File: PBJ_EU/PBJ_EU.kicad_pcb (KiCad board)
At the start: 2 copper layers, 111.4 x 128.5 mm, 75 parts, among them J1 Molex_47257, J10 Conn_02x05_Odd_Even, J2 Molex_47257, J3 Molex_47257, J4 Molex_47257, J7 Conn_02x05_Odd_Even, J9 Conn_02x08_Odd_Even_Female, SW1 SW_SPDT, SW2 SW_SPDT, SW5 SW_DPST, U1 TL072, U2 TL072, U7 MC7805CTG

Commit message: Version 4.10
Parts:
- U7: footprint Package_TO_SOT_THT:TO-220-3_Vertical -> Package_TO_SOT_THT:TO-220-3_Horizontal_TabDown
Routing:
- net +12V: track 0.00 -> 182.8 mm, vias 0 -> 5
- added copper zone on B.Cu, net GND
- removed copper zone on B.Cu, net +12V

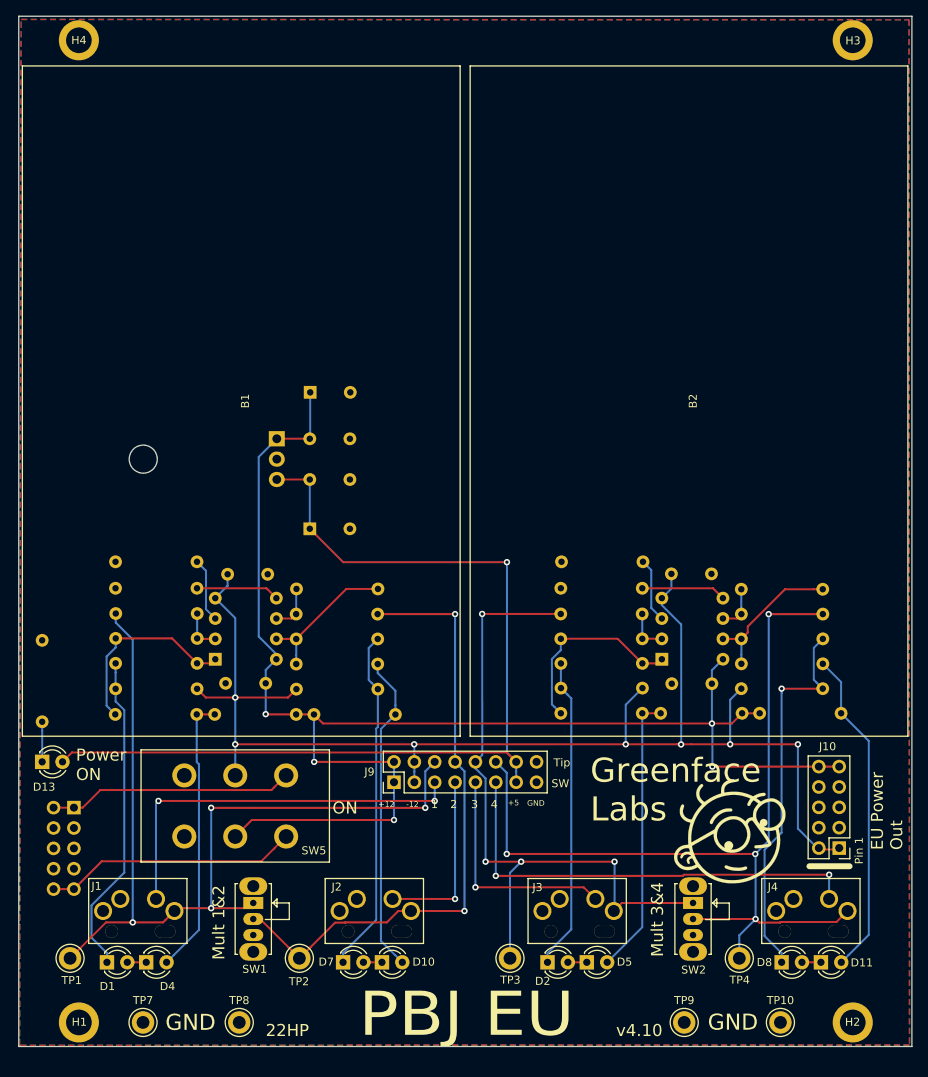
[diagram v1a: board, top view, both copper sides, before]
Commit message: v5.2
Adds LCSC build support. Fixes to monitor circuitry.
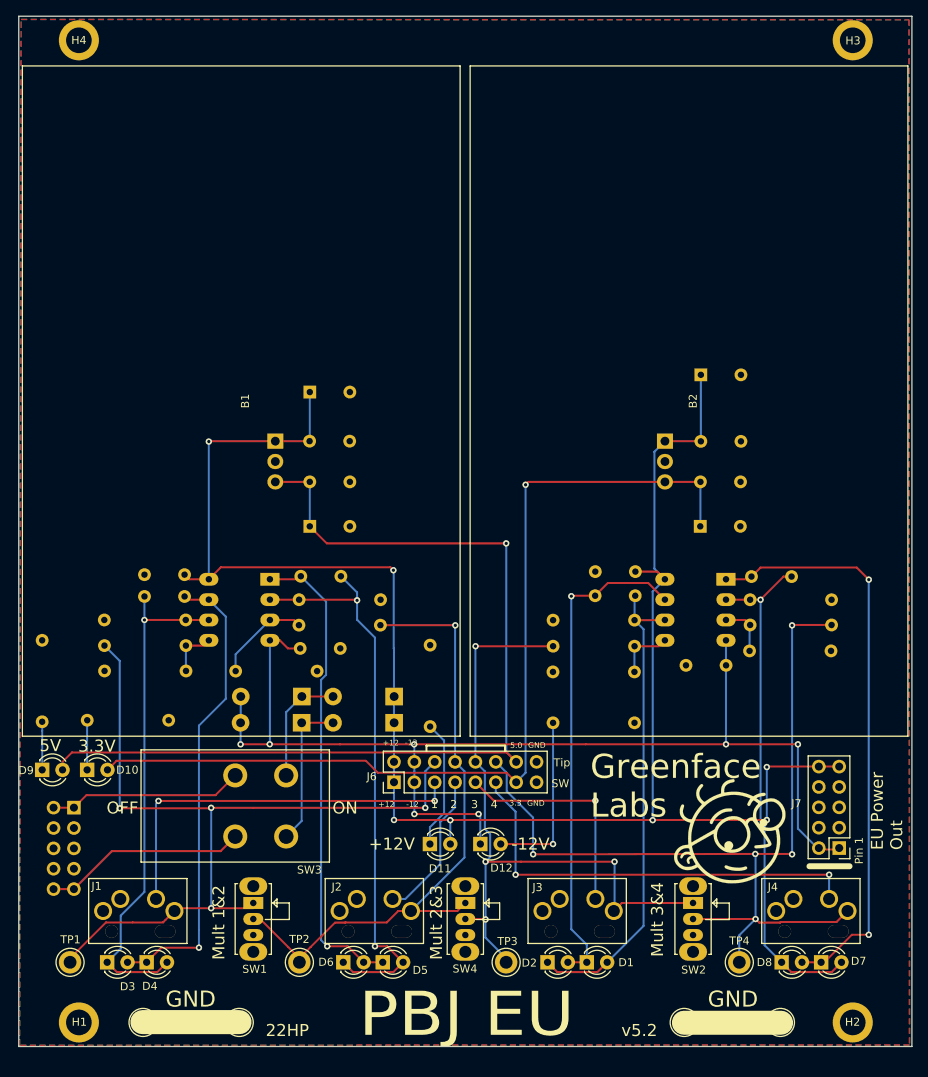
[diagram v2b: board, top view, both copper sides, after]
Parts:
- removed D13: GREEN LED, LED_THT:LED_D3.0mm
- removed J10: Conn_02x05_Odd_Even, Connector_PinHeader_2.54mm:PinHeader_2x05_P2.54mm_Vertical
- removed J9: Conn_02x08_Odd_Even_Female, Connector_PinHeader_2.54mm:PinHeader_2x08_P2.54mm_Vertical
- removed R17, R40, R41: 3.32M, Resistor_THT:R_Axial_DIN0207_L6.3mm_D2.5mm_P10.16mm_Horizontal
- removed R19, R20, R31, R32, R44, R45: 10K, Resistor_THT:R_Axial_DIN0207_L6.3mm_D2.5mm_P10.16mm_Horizontal
- removed R22, R23, R43, R47, R48: 2.2K, Resistor_THT:R_Axial_DIN0207_L6.3mm_D2.5mm_P10.16mm_Horizontal
- removed R34, R35: 1.00M, Resistor_THT:R_Axial_DIN0207_L6.3mm_D2.5mm_P10.16mm_Horizontal
- removed R37, R38: 1K, Resistor_THT:R_Axial_DIN0207_L6.3mm_D2.5mm_P10.16mm_Horizontal
- removed SW5: SW_DPST, sputterizer:S202031MS02Q
- removed TP10, TP9: TestPoint, TestPoint:TestPoint_Keystone_5005-5009_Compact
- removed U7: MC7805CTG, Package_TO_SOT_THT:TO-220-3_Horizontal_TabDown
- added C10: .1uF, Capacitor_THT:C_Rect_L7.0mm_W2.0mm_P5.00mm, B.Cu at (116.9, 99.3)
- added C11: .1uF, Capacitor_THT:C_Rect_L7.0mm_W2.0mm_P5.00mm, B.Cu at (123.2, 111.0)
- added C12: 10uF, Capacitor_THT:CP_Radial_Tantal_D5.0mm_P5.00mm, B.Cu at (125.0, 93.6)
- added C13: 10nF, Capacitor_THT:C_Rect_L7.0mm_W2.0mm_P5.00mm, B.Cu at (116.9, 102.3)
- added C14: 10nF, Capacitor_THT:C_Rect_L7.0mm_W2.0mm_P5.00mm, B.Cu at (55.7, 102.4)
- added C15: 10nF, Capacitor_THT:C_Rect_L7.0mm_W2.0mm_P5.00mm, B.Cu at (80.2, 99.8)
- added C16: 10nF, Capacitor_THT:C_Rect_L7.0mm_W2.0mm_P5.00mm, B.Cu at (136.4, 99.9)
- added C9: .1uF, Capacitor_THT:C_Rect_L7.0mm_W2.0mm_P5.00mm, B.Cu at (125.0, 88.1)
- added D12: GREEN LED, LED_THT:LED_D3.0mm, F.Cu at (97.6, 133.2)
- added D18: SB120, Diode_THT:D_DO-41_SOD81_P7.62mm_Horizontal, B.Cu at (86.8, 118.1)
- added D19: SB120, Diode_THT:D_DO-41_SOD81_P7.62mm_Horizontal, B.Cu at (86.8, 114.8)
- added D20: SB120, Diode_THT:D_DO-41_SOD81_P7.62mm_Horizontal, B.Cu at (75.3, 118.1)
- added D21: SB120, Diode_THT:D_DO-41_SOD81_P7.62mm_Horizontal, B.Cu at (75.3, 114.8)
- added D3: RED LED, LED_THT:LED_D3.0mm, F.Cu at (51.0, 148.0)
- added D6: RED LED, LED_THT:LED_D3.0mm, F.Cu at (80.5, 148.0)
- added D9: GREEN LED, LED_THT:LED_D3.0mm, F.Cu at (42.9, 124.0)
- added J5: Conn_02x05_Odd_Even, Connector_PinHeader_2.54mm:PinHeader_2x05_P2.54mm_Vertical, B.Cu at (46.9, 128.7)
- added J6: Conn_02x08_Odd_Even_Female, Connector_PinHeader_2.54mm:PinHeader_2x08_P2.54mm_Vertical, F.Cu at (86.8, 125.5)
- added R12: 1M, Resistor_THT:R_Axial_DIN0207_L6.3mm_D2.5mm_P10.16mm_Horizontal, B.Cu at (67.0, 111.7)
- added R15: 2.2K, Resistor_THT:R_Axial_DIN0207_L6.3mm_D2.5mm_P10.16mm_Horizontal, B.Cu at (91.3, 118.6)
- added R5: 2.2K, Resistor_THT:R_Axial_DIN0207_L6.3mm_D2.5mm_P10.16mm_Horizontal, B.Cu at (42.9, 118.0)
- added R6: 2.2K, Resistor_THT:R_Axial_DIN0207_L6.3mm_D2.5mm_P10.16mm_Horizontal, B.Cu at (60.9, 108.5)
- added R9: 2.2K, Resistor_THT:R_Axial_DIN0207_L6.3mm_D2.5mm_P10.16mm_Horizontal, B.Cu at (131.2, 105.9)
- added SW3: SW_DPST, sputterizer:S202031MS02Q, F.Cu at (67.0, 128.5)
- added SW4: SW_SPDT, Button_Switch_THT:SW_Slide_1P2T_CK_OS102011MS2Q, F.Cu at (95.7, 140.6)
- added TP5: TestPoint, TestPoint:TestPoint_Keystone_5005-5009_Compact, F.Cu at (123.0, 155.5)
- added TP6: TestPoint, TestPoint:TestPoint_Keystone_5005-5009_Compact, F.Cu at (135.0, 155.5)
- added U3: MC7805CTG, Package_TO_SOT_THT:TO-220-3_Vertical, B.Cu at (72.0, 83.0)
- added U4: MIC29150-3.3WT, Package_TO_SOT_THT:TO-220-3_Vertical, B.Cu at (120.6, 83.0)
- C2: value 10uF -> .33uF; footprint Capacitor_THT:CP_Radial_Tantal_D5.0mm_P5.00mm -> Capacitor_THT:C_Rect_L7.0mm_W2.0mm_P5.00mm
- C3: value .33uF -> .1uF
- C4, C5: value .1uF -> 10uF; footprint Capacitor_THT:C_Rect_L7.0mm_W2.0mm_P5.00mm -> Capacitor_THT:CP_Radial_Tantal_D5.0mm_P5.00mm
- C8: value .1uF -> .33uF
- D1, D7: value RED LED -> BLUE LED
- D10, D11: value BLUE LED -> GREEN LED
- J7: moved to F.Cu
- R1, R2, R3, R4: value 750K -> 2.2K
- R10, R11: value 1.00M -> 1M
- R13: value 1K -> 1M
- R14: value 1K -> 2.2K
- R16: value 3.32M -> 2.2K
- R7, R8: value 10K -> 2.2K
- U1, U2: value TL072 -> TL032IP; footprint Package_DIP:DIP-8_W7.62mm -> Package_DIP:DIP-8_W7.62mm_Socket_LongPads
- moved J7 95.6 mm to (142.3, 133.8)
- moved R14 69.6 mm to (48.5, 117.8), turned to 0 degrees
- moved R13 68.9 mm to (131.2, 109.2), turned to 0 degrees
- moved R2 67.6 mm to (50.7, 105.3), turned to 0 degrees
- moved C6 67.2 mm to (60.7, 99.7)
- moved R10 65.1 mm to (116.8, 111.8), turned to 180 degrees
- moved R7 64.9 mm to (116.8, 108.6), turned to 180 degrees
- moved D1 59.8 mm to (110.8, 148.0)
- moved D7 59.6 mm to (140.1, 148.0)
- moved C5 59.5 mm to (125.1, 74.7), turned to 0 degrees
- moved D11 50.9 mm to (91.3, 133.2)
- moved C8 49.0 mm to (125.1, 83.0)
- moved R11 47.3 mm to (60.9, 111.7), turned to 180 degrees
- moved C7 47.2 mm to (80.1, 108.8)
- moved R16 45.6 mm to (106.6, 118.1), turned to 0 degrees
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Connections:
- C2 pad 1: +5V -> +12V
- C3 pad 1: +12V -> +5V
- C4 pad 1: +12V -> +5V
- C5 pad 1: GND -> +12V
- C5 pad 2: -12V -> GND
- C8 pad 1: +5V -> +12V
- D1 pad 2: GND -> Net-(D1-Pad2)
- D10 pad 1: GND -> Net-(D10-Pad1)
- D10 pad 2: Net-(D10-Pad2) -> +3V3
- D11 pad 1: GND -> Net-(D11-Pad1)
- D11 pad 2: Net-(D11-Pad2) -> +12V
- D2 pad 1: Net-(D2-Pad1) -> Net-(D1-Pad2)
- D2 pad 2: GND -> Net-(D1-Pad1)
- D4 pad 1: GND -> Net-(D3-Pad2)
- D4 pad 2: Net-(D4-Pad2) -> Net-(D3-Pad1)
- D5 pad 1: GND -> Net-(D5-Pad1)
- D7 pad 2: GND -> Net-(D7-Pad2)
- D8 pad 1: Net-(D8-Pad1) -> Net-(D7-Pad2)
- D8 pad 2: GND -> Net-(D7-Pad1)
- J7 pad 1: Net-(J7-Pad1) -> -12V
- J7 pad 10: Net-(J7-Pad10) -> +12V
- J7 pad 2: Net-(J7-Pad1) -> -12V
- J7 pad 9: Net-(J7-Pad10) -> +12V
- R1 pad 1: Net-(R1-Pad1) -> GND
- R1 pad 2: GND -> Net-(D1-Pad2)
- R10 pad 1: Tip1 -> Net-(R10-Pad1)
- R10 pad 2: Net-(R10-Pad2) -> GND
- R11 pad 1: Tip3 -> Net-(R11-Pad1)
- R11 pad 2: Net-(R11-Pad2) -> GND
- R13 pad 2: Net-(D1-Pad1) -> GND
- R14 pad 1: Net-(R14-Pad1) -> Net-(D10-Pad1)
- R14 pad 2: Net-(D2-Pad1) -> GND
- R16 pad 1: Net-(R10-Pad2) -> Net-(D12-Pad2)
- R16 pad 2: Net-(R13-Pad1) -> GND
- R2 pad 1: Net-(R2-Pad1) -> GND
- R2 pad 2: GND -> Net-(D3-Pad1)
- R3 pad 1: Net-(R3-Pad1) -> GND
- R3 pad 2: GND -> Net-(D5-Pad2)
- R4 pad 1: Net-(R4-Pad1) -> GND
- R4 pad 2: GND -> Net-(D7-Pad2)
- R7 pad 1: Net-(D1-Pad1) -> Net-(R10-Pad1)
- R7 pad 2: -12V -> Tip3
- R8 pad 1: Net-(D2-Pad1) -> Net-(R12-Pad1)
- R8 pad 2: -12V -> Tip2
- U1 pad 1: Net-(R13-Pad1) -> Net-(D5-Pad1)
- U1 pad 2: Net-(R10-Pad2) -> Net-(D5-Pad2)
- U1 pad 3: Net-(R1-Pad1) -> Net-(R12-Pad1)
- U1 pad 5: Net-(R3-Pad1) -> Net-(R11-Pad1)
- U1 pad 6: Net-(R34-Pad2) -> Net-(D3-Pad1)
- U1 pad 7: Net-(R37-Pad1) -> Net-(D3-Pad2)
- U2 pad 1: Net-(R14-Pad1) -> Net-(D7-Pad1)
- U2 pad 2: Net-(R11-Pad2) -> Net-(D7-Pad2)
- U2 pad 3: Net-(R2-Pad1) -> Net-(R13-Pad1)
- U2 pad 5: Net-(R4-Pad1) -> Net-(R10-Pad1)
- U2 pad 6: Net-(R35-Pad2) -> Net-(D1-Pad2)
- U2 pad 7: Net-(R38-Pad1) -> Net-(D1-Pad1)
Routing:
- net +3V3: track 0.00 -> 117.7 mm, vias 0 -> 1
- net Net-(D7-Pad2): track 0.00 -> 64.1 mm, vias 0 -> 1
- net Net-(D3-Pad1): track 0.00 -> 64.1 mm, vias 0 -> 1
- net Net-(D1-Pad2): track 0.00 -> 60.2 mm
- net Net-(D5-Pad1): track 0.00 -> 59.7 mm, vias 0 -> 1
- net Net-(D3-Pad2): track 0.00 -> 58.5 mm, vias 0 -> 1
- net Net-(D8-Pad1): track 48.2 -> 0.00 mm, vias 1 -> 0
- net +12V: track 182.8 -> 225.1 mm, vias 5 -> 7
- net Net-(D11-Pad2): track 41.0 -> 0.00 mm
- net Net-(D10-Pad2): track 40.0 -> 0.00 mm
- net Net-(D2-Pad1): track 39.0 -> 0.00 mm
- net Net-(D5-Pad2): track 35.2 -> 71.6 mm, vias 0 -> 2
- net Net-(D4-Pad2): track 34.9 -> 0.00 mm
- net Net-(J7-Pad10): track 31.7 -> 0.00 mm
- net Net-(J7-Pad1): track 30.7 -> 0.00 mm
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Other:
- board text added: "+12V"
- board text added: "-12V"
- board text added: "3.3"
- board text added: "3.3V"
- board text added: "5.0"
- board text added: "5V"
- board text added: "Either Way"
- board text added: "Mult 2&3"
- board text added: "OFF"
- board text added: "S/N 5.2."
- board text added: "v5.2"
- board text removed: "+5"
- board text removed: "Note inverted orientation of U1 & U2"
- board text removed: "Power ON"
- board text removed: "SN"
- board text removed: "v4.10"

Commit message: lm317 experiment checkin
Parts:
- removed C3, C9: .1uF, Capacitor_THT:C_Rect_L7.0mm_W2.0mm_P5.00mm
- added R17: 620, Resistor_THT:R_Axial_DIN0207_L6.3mm_D2.5mm_P10.16mm_Horizontal, B.Cu at (56.3, 87.6)
- added R18: 620, Resistor_THT:R_Axial_DIN0207_L6.3mm_D2.5mm_P10.16mm_Horizontal, B.Cu at (83.2, 87.6)
- added RV1: 5K, Potentiometer_THT:Potentiometer_Bourns_3296W_Vertical, B.Cu at (56.3, 92.0)
- added RV2: 5K, Potentiometer_THT:Potentiometer_Bourns_3296W_Vertical, B.Cu at (83.1, 92.0)
- C1, C5: footprint Capacitor_THT:CP_Radial_Tantal_D5.0mm_P5.00mm -> Capacitor_THT:C_Radial_D5.0mm_H11.0mm_P2.00mm
- C12, C4: value 10uF -> 22uF; footprint Capacitor_THT:CP_Radial_Tantal_D5.0mm_P5.00mm -> Capacitor_THT:C_Radial_D5.0mm_H11.0mm_P2.00mm
- C2, C8: value .33uF -> .1uF
- D10: value GREEN LED -> YELLOW LED
- D11: value GREEN LED -> RED LED
- D12: value GREEN LED -> BLUE LED
- U3: value MC7805CTG -> LM317_TO-220
- U4: value MIC29150-3.3WT -> LM317_TO-220
- moved C12 47.4 mm to (77.6, 92.0), turned to 180 degrees
- moved C8 44.7 mm to (80.6, 87.6), turned to 180 degrees
- moved C5 36.1 mm to (93.4, 92.0)
- moved U4 34.9 mm to (85.7, 84.5), turned to 180 degrees
- moved C4 26.7 mm to (49.7, 91.0), turned to -90 degrees
- moved C2 23.0 mm to (53.7, 87.6), turned to 180 degrees
- moved C1 18.1 mm to (66.4, 92.0)
- moved U3 13.3 mm to (58.8, 84.5), turned to 180 degrees
- moved D3 0.50 mm to (51.5, 148.0)
- moved D4 0.50 mm to (56.5, 148.0)
- moved J1 0.50 mm to (55.4, 141.6)
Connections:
- C1 pad 1: +12V -> Net-(C1-Pad1)
- C5 pad 1: +12V -> Net-(R18-Pad2)
- U3 pad 1: +12V -> Net-(C1-Pad1)
- U3 pad 2: GND -> +5V
- U3 pad 3: +5V -> +12V
- U4 pad 1: +12V -> Net-(R18-Pad2)
- U4 pad 2: GND -> +3V3
- U4 pad 3: +3V3 -> +12V
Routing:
- net +12V: track 225.1 -> 7.42 mm, vias 7 -> 0
- net Net-(R18-Pad2): track 0.00 -> 19.7 mm
- net Net-(C1-Pad1): track 0.00 -> 19.5 mm
- net +5V: track 120.5 -> 128.3 mm, vias 1 -> 2
- net -12V: track 142.9 -> 150.5 mm
- net +3V3: track 117.7 -> 123.3 mm
- net GND: track 0.00 -> 1.99 mm, vias 0 -> 1
- net Net-(C14-Pad1): track 64.1 -> 63.5 mm
- added copper zone on F.Cu, net +12V
- removed copper zone on F.Cu, net GND
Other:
- board text added: "+3.3V"
- board text added: "+5V"
- board text added: "POWER IN"
- board text added: "S/N 6.0."
- board text added: "v6.0"
- board text added: "{dblquote}Argh Ptoo{dblquote}"
- board text removed: "S/N 5.2."
- board text removed: "v5.2"

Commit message: Uses LM317 for regulators now.
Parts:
- C1, C12, C4, C5: footprint Capacitor_THT:C_Radial_D5.0mm_H11.0mm_P2.00mm -> Capacitor_THT:CP_Radial_D5.0mm_P2.00mm
- U1, U2: value TL032IP -> TL072
